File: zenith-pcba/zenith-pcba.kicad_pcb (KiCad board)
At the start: 2 copper layers, 28 parts, among them SW1 G4R152312, U1 XC7A50T-CSG325, U2 K4B4G1646E-BCNB, U3 CH347T, U4 AP63203WU, U5 TXS0101DB, U6 TXS0101DB, U7 TXS0101DB, U8 TXS0101DB, X1 SX5B8.000F1520F30

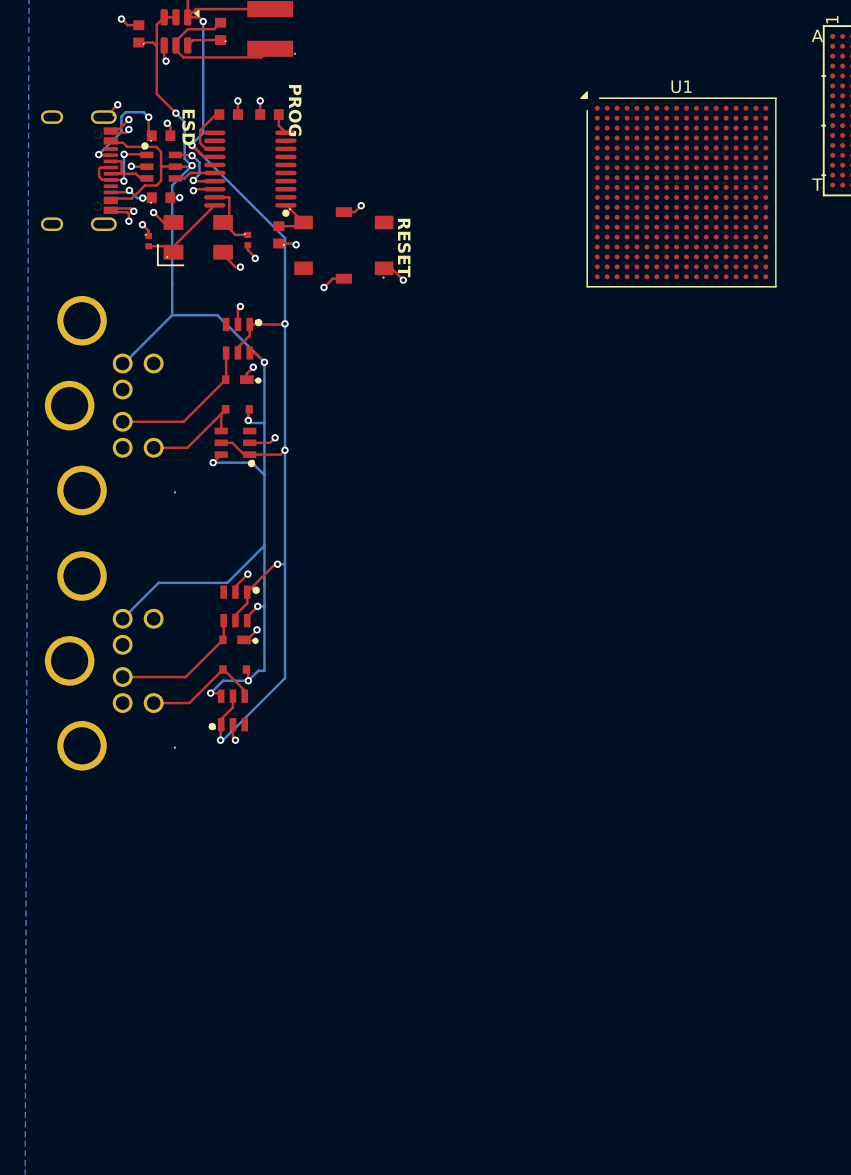
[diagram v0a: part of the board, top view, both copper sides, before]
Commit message: feat(pcba): sd card schematic
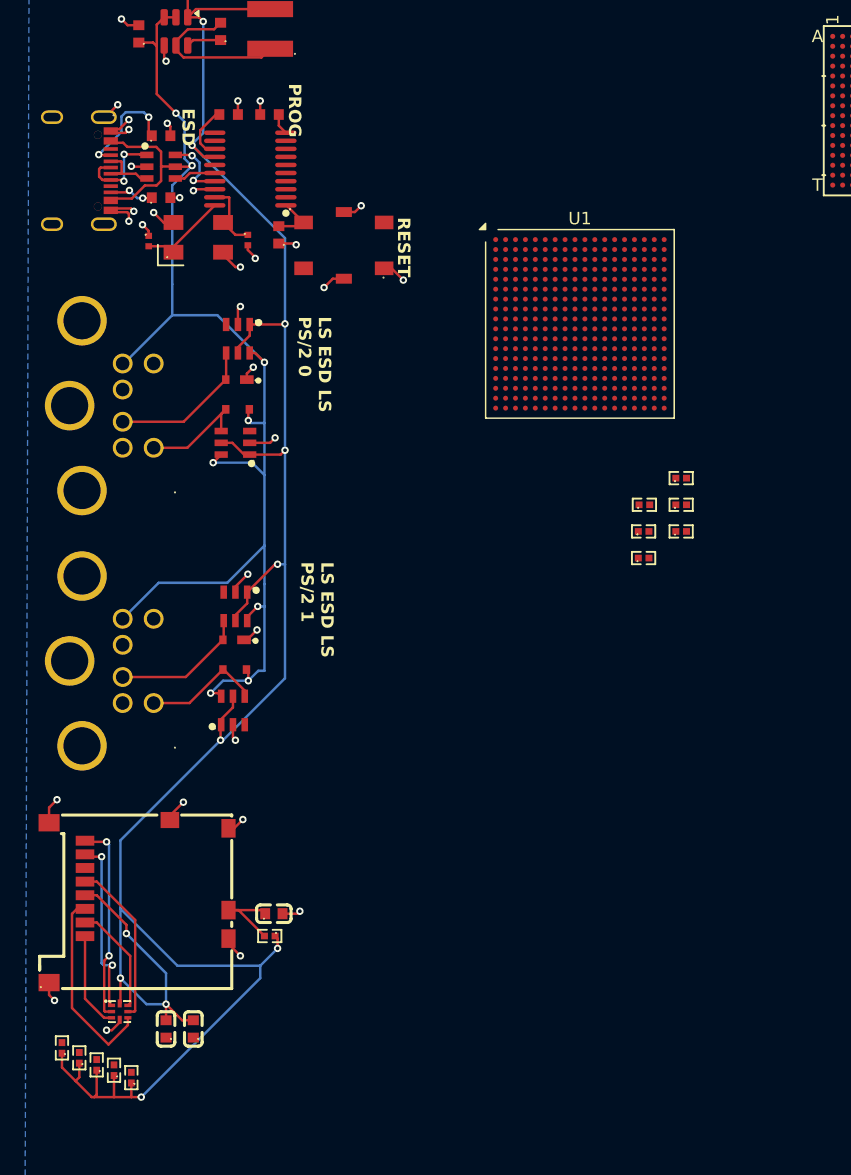
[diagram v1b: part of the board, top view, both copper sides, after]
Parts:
- added C10: CC0603MRX5R7BB106, easyeda2kicad:C0603, F.Cu at (70.6, 135.7)
- added C8: CL10B104KA8NNNC, easyeda2kicad:C0603, F.Cu at (77.1, 126.4)
- added C9: CL10B104KA8NNNC, easyeda2kicad:C0603, F.Cu at (68.4, 135.7)
- added Card1: 5025700893, easyeda2kicad:TF-SMD_5025700893, F.Cu at (66.2, 125.4)
- added D4: TPD6E004RSER, easyeda2kicad:UQFN-8_L1.5-W1.5-P0.50-TL, F.Cu at (64.7, 134.3)
- added R10: RC0402FR-0722R1L, easyeda2kicad:R0402, F.Cu at (107.0, 93.4)
- added R11: RC0402FR-0722R1L, easyeda2kicad:R0402, F.Cu at (106.9, 95.5)
- added R12: RC0402FR-0722R1L, easyeda2kicad:R0402, F.Cu at (106.9, 97.7)
- added R13: RC0402FR-0722R1L, easyeda2kicad:R0402, F.Cu at (110.0, 91.2)
- added R14: RC0402FR-0722R1L, easyeda2kicad:R0402, F.Cu at (110.0, 93.4)
- added R15: RC0402FR-0722R1L, easyeda2kicad:R0402, F.Cu at (110.0, 95.5)
- added R16: RC0402FR-0710KL, easyeda2kicad:R0402, F.Cu at (76.8, 128.2)
- added R5: RC0402FR-0710KL, easyeda2kicad:R0402, F.Cu at (62.8, 138.6)
- added R6: RC0402FR-0710KL, easyeda2kicad:R0402, F.Cu at (64.2, 139.0)
- added R7: RC0402FR-0710KL, easyeda2kicad:R0402, F.Cu at (65.6, 139.6)
- added R8: RC0402FR-0710KL, easyeda2kicad:R0402, F.Cu at (60.0, 137.2)
- added R9: RC0402FR-0710KL, easyeda2kicad:R0402, F.Cu at (61.4, 138.0)
- moved U1 13.4 mm to (101.8, 78.8)
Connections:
- U1 pad K3: unconnected-(U1B-IO_L4P_T0_34-PadK3) -> Net-(U1B-IO_L4P_T0_34)
- U1 pad L2: unconnected-(U1B-IO_L4N_T0_34-PadL2) -> Net-(U1B-IO_L4N_T0_34)
- U1 pad L3: unconnected-(U1B-IO_L5N_T0_34-PadL3) -> Net-(U1B-IO_L5N_T0_34)
- U1 pad L4: unconnected-(U1B-IO_L5P_T0_34-PadL4) -> Net-(U1B-IO_L5P_T0_34)
- U1 pad L5: unconnected-(U1B-IO_L6P_T0_34-PadL5) -> Net-(U1B-IO_L6P_T0_34)
- U1 pad M2: unconnected-(U1B-IO_L7P_T1_34-PadM2) -> /IO/SDSW
- U1 pad M5: unconnected-(U1B-IO_L6N_T0_VREF_34-PadM5) -> Net-(U1B-IO_L6N_T0_VREF_34)
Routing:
- net VCC3.3: track 99.6 -> 191.3 mm, vias 6 -> 11
- net /IO/SDDAT1: track 0.00 -> 16.3 mm, vias 0 -> 2
- net /IO/SDCMD: track 0.00 -> 15.8 mm
- net /IO/SDDAT0: track 0.00 -> 14.5 mm, vias 0 -> 2
- net /IO/SDCLK: track 0.00 -> 13.3 mm
- net GND: track 43.5 -> 55.4 mm, vias 28 -> 35
- net /IO/SDDAT3: track 0.00 -> 8.84 mm
- net /IO/SDDAT2: track 0.00 -> 7.83 mm
- net /IO/SDSW: track 0.00 -> 6.85 mm
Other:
- board text added: "LS ESD LS PS/2 0"
- board text added: "LS ESD LS PS/2 1"

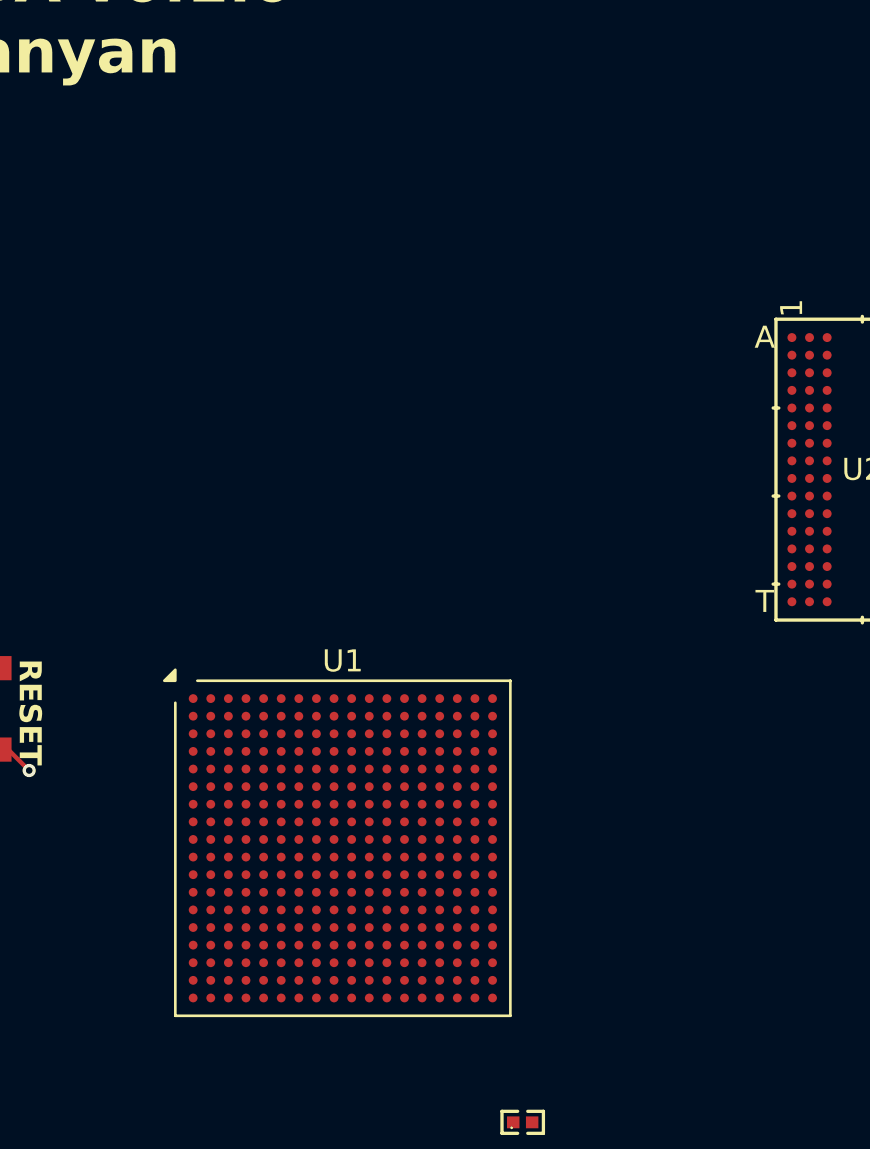
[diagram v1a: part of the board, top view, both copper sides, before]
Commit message: feat(pcba): migrate to kintex fpga
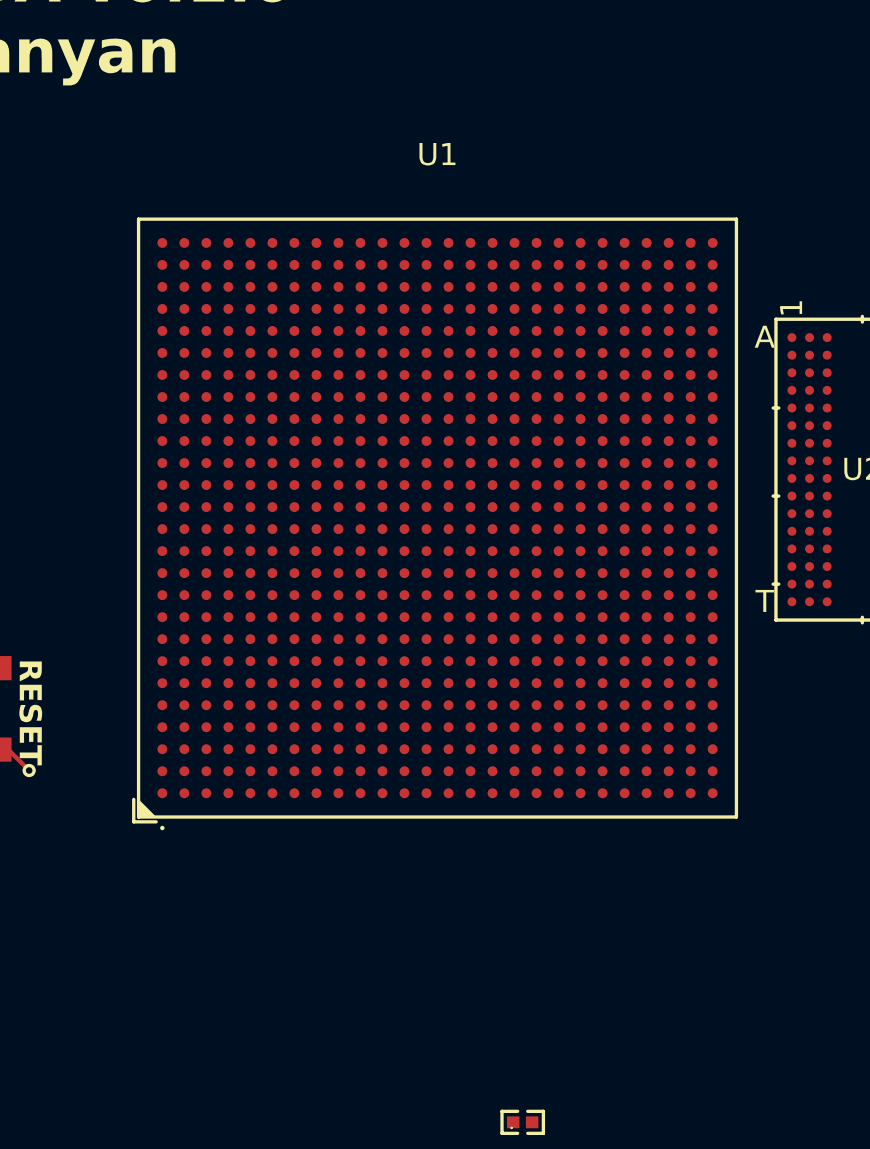
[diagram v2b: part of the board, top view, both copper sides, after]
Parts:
- U1: value XC7A50T-CSG325 -> XC7K70T-FBG676; footprint Package_BGA:Xilinx_CSG325 -> easyeda2kicad:FBGA-676_L27.0-W27.0-R26-C26-P1.00-BL
- moved U1 15.6 mm to (106.1, 63.8)
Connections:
- R10 pad 2: Net-(U1B-IO_L4P_T0_34) -> Net-(U1D-IO_L4P_T0_33)
- R11 pad 2: Net-(U1B-IO_L4N_T0_34) -> Net-(U1D-IO_L4N_T0_33)
- R12 pad 2: Net-(U1B-IO_L5P_T0_34) -> Net-(U1D-IO_L5P_T0_33)
- R13 pad 2: Net-(U1B-IO_L5N_T0_34) -> Net-(U1D-IO_L5N_T0_33)
- R14 pad 2: Net-(U1B-IO_L6P_T0_34) -> Net-(U1D-IO_L6P_T0_33)
- R15 pad 2: Net-(U1B-IO_L6N_T0_VREF_34) -> Net-(U1D-IO_L6N_T0_VREF_33)
- U1 pad E10: VCC3.3 -> unconnected-(U1C-IO_L12P_T1_MRCC_16-PadE10)
- U1 pad E11: VCC1.8 -> unconnected-(U1C-IO_L14P_T2_SRCC_16-PadE11)
- U1 pad F11: VCC1.0 -> unconnected-(U1H-GND-PadF11)
- U1 pad F7: VCC1.0 -> unconnected-(U1H-GND-PadF7)
- U1 pad F8: Net-(U1E-TCK_0) -> unconnected-(U1C-IO_L7N_T1_16-PadF8)
- U1 pad F9: VCC1.0 -> unconnected-(U1C-IO_L7P_T1_16-PadF9)
- U1 pad G10: VCC1.0 -> unconnected-(U1C-IO_L2P_T0_16-PadG10)
- U1 pad G12: VCC1.8 -> unconnected-(U1C-IO_L16P_T2_16-PadG12)
- U1 pad G8: VCC1.0 -> unconnected-(U1H-GND-PadG8)
- U1 pad H11: VCC1.0 -> unconnected-(U1C-IO_L6N_T0_VREF_16-PadH11)
- U1 pad H13: VCC1.8 -> unconnected-(U1C-IO_L3N_T0_DQS_16-PadH13)
- U1 pad H7: VCC1.0 -> unconnected-(U1H-GND-PadH7)
- U1 pad H9: VCC1.0 -> unconnected-(U1C-IO_L1P_T0_16-PadH9)
- U1 pad J10: VCC1.8 -> unconnected-(U1C-IO_L4N_T0_16-PadJ10)
- U1 pad J12: VCC1.0 -> unconnected-(U1H-GND-PadJ12)
- U1 pad J4: Net-(U1B-IO_L2N_T0_34) -> unconnected-(U1E-MGTXRXP3_115-PadJ4)
- U1 pad J5: Net-(U1B-IO_L2P_T0_34) -> unconnected-(U1H-GND-PadJ5)
- U1 pad J8: VCC1.0 -> unconnected-(U1C-IO_0_16-PadJ8)
- U1 pad J9: GND -> unconnected-(U1H-VCCINT-PadJ9)
- U1 pad K1: Net-(U1B-IO_L3N_T0_DQS_34) -> unconnected-(U1E-MGTXTXN2_115-PadK1)
- U1 pad K10: GND -> unconnected-(U1H-VCCINT-PadK10)
- U1 pad K11: VCC1.0 -> unconnected-(U1H-GND-PadK11)
- U1 pad K13: VCC1.8 -> unconnected-(U1H-GND-PadK13)
- U1 pad K2: Net-(U1B-IO_L3P_T0_DQS_34) -> unconnected-(U1E-MGTXTXP2_115-PadK2)
- U1 pad K3: Net-(U1B-IO_L4P_T0_34) -> unconnected-(U1H-GND-PadK3)
- U1 pad K5: UARTTX -> unconnected-(U1E-MGTREFCLK1N_115-PadK5)
- U1 pad K6: UARTRX -> unconnected-(U1E-MGTREFCLK1P_115-PadK6)
- U1 pad K7: VCC1.0 -> unconnected-(U1H-GND-PadK7)
- U1 pad K9: GND -> unconnected-(U1H-GND-PadK9)
- U1 pad L10: GND -> unconnected-(U1H-GND-PadL10)
- U1 pad L12: VCC1.0 -> unconnected-(U1H-GND-PadL12)
- U1 pad L2: Net-(U1B-IO_L4N_T0_34) -> unconnected-(U1F-MGTAVTT-PadL2)
- U1 pad L3: Net-(U1B-IO_L5N_T0_34) -> unconnected-(U1E-MGTXRXN2_115-PadL3)
- U1 pad L4: Net-(U1B-IO_L5P_T0_34) -> unconnected-(U1E-MGTXRXP2_115-PadL4)
- U1 pad L5: Net-(U1B-IO_L6P_T0_34) -> unconnected-(U1H-GND-PadL5)
- U1 pad L6: VCC3.3 -> unconnected-(U1F-MGTAVCC-PadL6)
- U1 pad L7: unconnected-(U1F-GND-PadL7) -> VCC3.3
- U1 pad L8: VCC1.0 -> Net-(U1G-TCK_0)
- U1 pad L9: GND -> unconnected-(U1H-VCCINT-PadL9)
- U1 pad M11: VCC1.0 -> unconnected-(U1H-GNDADC_0-PadM11)
- U1 pad M13: VCC1.8 -> unconnected-(U1H-GND-PadM13)
- U1 pad M2: /IO/SDSW -> unconnected-(U1E-MGTXTXP1_115-PadM2)
- U1 pad M3: VCC3.3 -> unconnected-(U1F-MGTAVTT-PadM3)
- U1 pad M5: Net-(U1B-IO_L6N_T0_VREF_34) -> unconnected-(U1F-MGTAVTTRCAL_115-PadM5)
- U1 pad M7: VCC1.0 -> unconnected-(U1H-GND-PadM7)
- U1 pad N10: VCC1.0 -> unconnected-(U1H-GND-PadN10)
- U1 pad N11: unconnected-(U1F-GND-PadN11) -> GND
- U1 pad N12: VCC1.0 -> GND
- U1 pad N8: VCC1.0 -> Net-(U1G-TMS_0)
- U1 pad P11: VCC1.0 -> GND
- U1 pad P12: unconnected-(U1F-GND-PadP12) -> GND
- U1 pad P13: VCC1.8 -> unconnected-(U1H-GND-PadP13)
- U1 pad P7: VCC3.3 -> unconnected-(U1G-CFGBVS_0-PadP7)
- U1 pad P9: VCC1.0 -> unconnected-(U1H-GND-PadP9)
- U1 pad R10: VCC3.3 -> unconnected-(U1H-GND-PadR10)
- U1 pad R4: VCC3.3 -> unconnected-(U1E-MGTXRXP0_115-PadR4)
- U1 pad R6: unconnected-(U1B-IO_25_34-PadR6) -> Net-(U1G-TDI_0)
- U1 pad R7: unconnected-(U1B-IO_L22P_T3_34-PadR7) -> Net-(U1G-TDO_0)
- U1 pad R8: Net-(U1E-TMS_0) -> unconnected-(U1H-GND-PadR8)
- U1 pad T1: VCC3.3 -> unconnected-(U1H-GND-PadT1)
- U1 pad T6: unconnected-(U1F-GND-PadT6) -> VCC3.3
- U1 pad T8: Net-(U1E-TDO_0) -> unconnected-(U1H-VCCAUX_IO_G0-PadT8)
- U1 pad T9: Net-(U1E-TDI_0) -> unconnected-(U1H-GND-PadT9)
- U1 pad V10: unconnected-(U1F-GND-PadV10) -> VCC3.3
- U1 pad V11: unconnected-(U1A-IO_L23N_T3_A02_D18_14-PadV11) -> UARTRX
- U1 pad V13: unconnected-(U1A-IO_L21N_T3_DQS_A06_D22_14-PadV13) -> (no net)
- U1 pad V14: unconnected-(U1A-IO_L20N_T3_A07_D23_14-PadV14) -> (no net)
- U1 pad V16: unconnected-(U1A-IO_L18P_T2_A12_D28_14-PadV16) -> (no net)
- U1 pad V17: unconnected-(U1A-IO_L18N_T2_A11_D27_14-PadV17) -> (no net)
- U1 pad V18: unconnected-(U1F-GND-PadV18) -> (no net)
- U1 pad V5: VCC3.3 -> unconnected-(U1H-GND-PadV5)
- U1 pad V7: unconnected-(U1B-IO_L24N_T3_34-PadV7) -> Net-(U1D-IO_L2N_T0_33)
- U1 pad V8: unconnected-(U1B-IO_L24P_T3_34-PadV8) -> Net-(U1D-IO_L2P_T0_33)
- U1 pad V9: unconnected-(U1A-IO_L24N_T3_A00_D16_14-PadV9) -> Net-(U1D-IO_L6P_T0_33)
- U3 pad 5: Net-(U1E-TMS_0) -> Net-(U1G-TMS_0)
- U3 pad 6: Net-(U1E-TCK_0) -> Net-(U1G-TCK_0)
- U3 pad 7: Net-(U1E-TDI_0) -> Net-(U1G-TDO_0)
- U3 pad 8: Net-(U1E-TDO_0) -> Net-(U1G-TDI_0)
- U5 pad 3: Net-(U1B-IO_L2P_T0_34) -> Net-(U1D-IO_L2P_T0_33)
- U6 pad 3: Net-(U1B-IO_L2N_T0_34) -> Net-(U1D-IO_L2N_T0_33)
- U7 pad 3: Net-(U1B-IO_L3P_T0_DQS_34) -> Net-(U1D-IO_L3P_T0_DQS_33)
- U8 pad 3: Net-(U1B-IO_L3N_T0_DQS_34) -> Net-(U1D-IO_L3N_T0_DQS_33)
